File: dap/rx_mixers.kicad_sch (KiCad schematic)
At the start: 2 parts, among them U7 SN74CBT3253, U8 SN74CBT3253

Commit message: general setup
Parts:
- removed U7, U8: SN74CBT3253, symbol Analog_Switch:SN74CBT3253
- added C1, C2: 47u, Capacitor_SMD:C_0805_2012Metric_Pad1.18x1.45mm_HandSolder, symbol Device:C_Polarized_Small_US
- added C10, C11, C16, C3, C4, C5, C6, C7, C8, C9: 0.1u, Capacitor_SMD:C_0805_2012Metric_Pad1.18x1.45mm_HandSolder, symbol Device:C_Small
- added C12, C13, C14, C15, C17, C18, C19, C20: 0.068u, Capacitor_SMD:C_0805_2012Metric_Pad1.18x1.45mm_HandSolder, symbol Device:C_Small
- added H1, H2, H3, H4: MountingHole, MountingHole:MountingHole_3.2mm_M3, symbol Mechanical:MountingHole
- added J12: Conn_01x05_Pin, Connector_PinHeader_2.54mm:PinHeader_1x05_P2.54mm_Vertical, symbol Connector:Conn_01x05_Pin
- added J13: I Channel SMA, Connector_Coaxial:SMA_Amphenol_132289_EdgeMount, symbol Connector:Conn_Coaxial
- added J14: Q Channel SMA, Connector_Coaxial:SMA_Amphenol_132289_EdgeMount, symbol Connector:Conn_Coaxial
- added J15: IF_input, Connector_Coaxial:SMA_Amphenol_132289_EdgeMount, symbol Connector:Conn_Coaxial
- added J16: rf_test, Connector_PinHeader_2.54mm:PinHeader_1x02_P2.54mm_Vertical, symbol Connector:Conn_01x02_Pin
- added J17: I_clk_test, Connector_PinHeader_2.54mm:PinHeader_1x02_P2.54mm_Vertical, symbol Connector:Conn_01x02_Pin
- added J18: Q_clk_test, Connector_PinHeader_2.54mm:PinHeader_1x02_P2.54mm_Vertical, symbol Connector:Conn_01x02_Pin
- added J19: Rx_Q_channel, Connector_Audio:Jack_3.5mm_CUI_SJ-3523-SMT_Horizontal, symbol audiojack3:AudioJack3
- added J20: Rx_I_channel, Connector_Audio:Jack_3.5mm_CUI_SJ-3523-SMT_Horizontal, symbol audiojack3:AudioJack3
- added J21: Tx_Q_channel, Connector_Audio:Jack_3.5mm_CUI_SJ-3523-SMT_Horizontal, symbol audiojack3:AudioJack3
- added J22: Tx_I_channel, Connector_Audio:Jack_3.5mm_CUI_SJ-3523-SMT_Horizontal, symbol audiojack3:AudioJack3
- added R1, R2: 2.2k, Resistor_SMD:R_0805_2012Metric_Pad1.20x1.40mm_HandSolder, symbol Device:R_Small_US
- added R3, R5, R6, R7: 1M, Resistor_SMD:R_0805_2012Metric_Pad1.20x1.40mm_HandSolder, symbol Device:R_Small_US
- added R4: 100, Resistor_SMD:R_0805_2012Metric_Pad1.20x1.40mm_HandSolder, symbol Device:R_Small_US
- added TR1: ADT4-6T, RF_Mini-Circuits:Mini-Circuits_CD637_H5.23mm, symbol Transformer:ADT4-6T
- added U11, U12, U13, U14: NC7SVU04P5X, Package_TO_SOT_SMD:SOT-353_SC-70-5, symbol 74xGxx:NC7SVU04P5X
- added U15, U16: SN74CBT3253, Package_SO:SOIC-16_3.9x9.9mm_P1.27mm, symbol Analog_Switch:SN74CBT3253
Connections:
- new net: C20.2, J22.T, U16.13 (2B4), U16.6 (1B1)
- new net: C12.2, J20.R, U15.10 (2B1), U15.3 (1B4)
- new net: C11.1, J15.1 (In), J16.1 (Pin_1)
- new net: C17.2, J22.R, U16.10 (2B1), U16.3 (1B4)
- new net: C13.2, J19.R, U15.11 (2B2), U15.4 (1B3)
- new net: C14.2, J19.T, U15.12 (2B3), U15.5 (1B2)
- new net: C15.2, J20.T, U15.13 (2B4), U15.6 (1B1)
- new net: TR1.4, U15.7 (1A), U16.7 (1A)
- new net: TR1.6, U15.9 (2A), U16.9 (2A)
- new net: C8.1, R6.1, U12.4
- new net: C6.2, R6.2, U12.2
- new net: C8.2, R7.2, U14.2
- new net: C19.2, J21.T, U16.12 (2B3), U16.5 (1B2)
- new net: C7.1, R3.1, U11.4
- new net: C7.2, R5.2, U13.2
- new net: C5.2, R3.2, U11.2
- new net: C5.1, J13.1 (In)
- new net: C18.2, J21.R, U16.11 (2B2), U16.4 (1B3)
- new net: C11.2, TR1.3
- new net: C6.1, J14.1 (In)
- new net +3.3V: C1.1, J12.2 (Pin_2), R1.1, R4.2
- new net +5V: C16.1, C9.1, J12.1 (Pin_1), U15.16 (VCC), U16.16 (VCC)
- new net GND: C1.2, C10.2, C12.1, C13.1, C14.1, C15.1, C16.2, C17.1, C18.1, C19.1, C2.2, C20.1, C3.2, C4.2, C9.2, J12.5 (Pin_5), J13.2 (Ext), J14.2 (Ext), J15.2 (Ext), J16.2 (Pin_2), J17.2 (Pin_2), J18.2 (Pin_2), J19.S, J20.S, J21.S, J22.S, R2.1, TR1.1, U11.3 (GND), U12.3 (GND), U13.3 (GND), U14.3 (GND), U15.8 (GND), U16.8 (GND)
- new net I_square: J17.1 (Pin_1), R5.1, U13.4, U15.14 (S0), U16.14 (S0)
- new net Q_square: J18.1 (Pin_1), R7.1, U14.4, U15.2 (S1), U16.2 (S1)
- new net Rx_control: J12.4 (Pin_4), U15.1 (1~{OE}), U15.15 (2~{OE})
- new net Tx_control: J12.3 (Pin_3), U16.1 (1~{OE}), U16.15 (2~{OE})
- new net V_inverter: C2.1, C3.1, C4.1, R4.1, U11.5 (VCC), U12.5 (VCC), U13.5 (VCC), U14.5 (VCC)
- new net bias: C10.1, R1.2, R2.2, TR1.5
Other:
- note added: "Detector Bias Circuit"
- note added: "Inverter Power"
- note added: "Power Flags"
- note added: "Power and Control"
- note added: "Quadrature Clocks"
- note added: "Receive Mixer"
- note added: "Transmit Mixer"

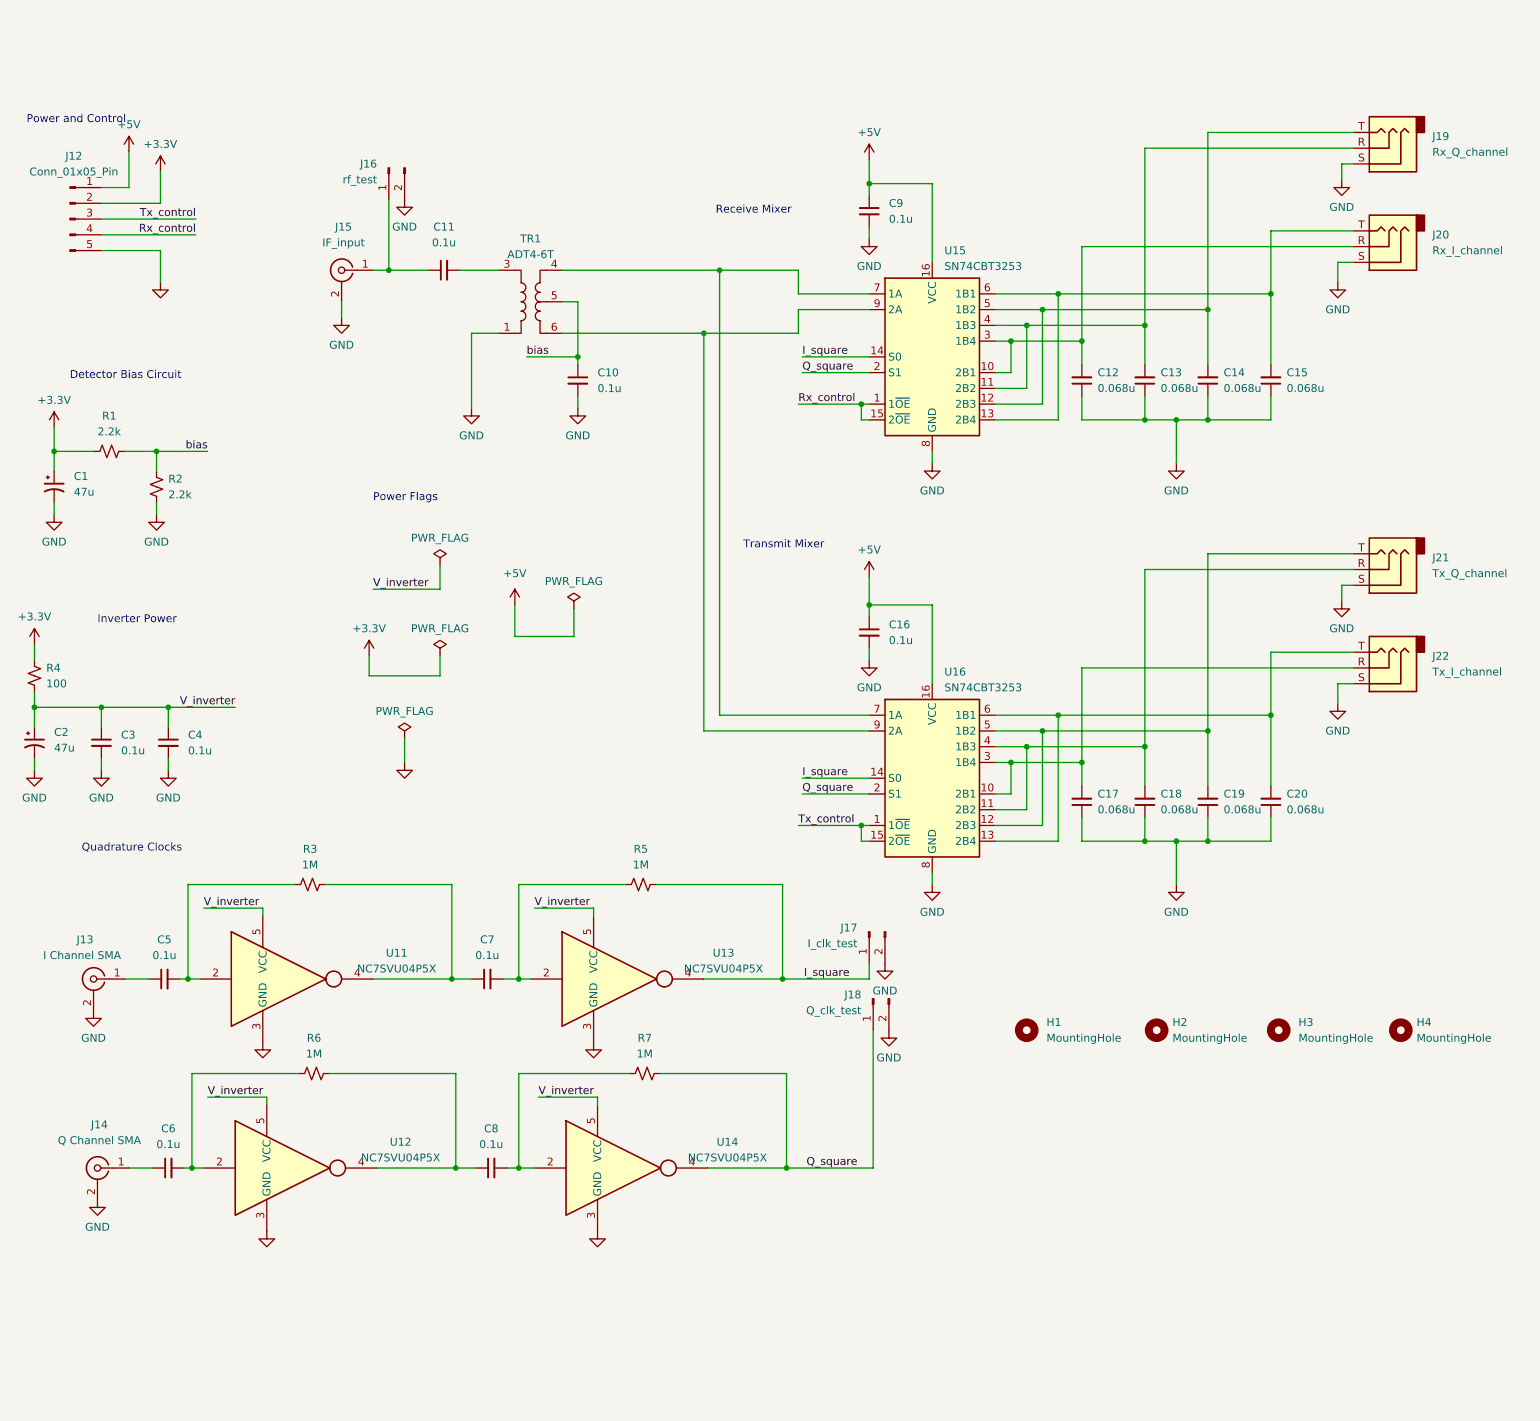
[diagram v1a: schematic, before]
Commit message: selected clocking scheme
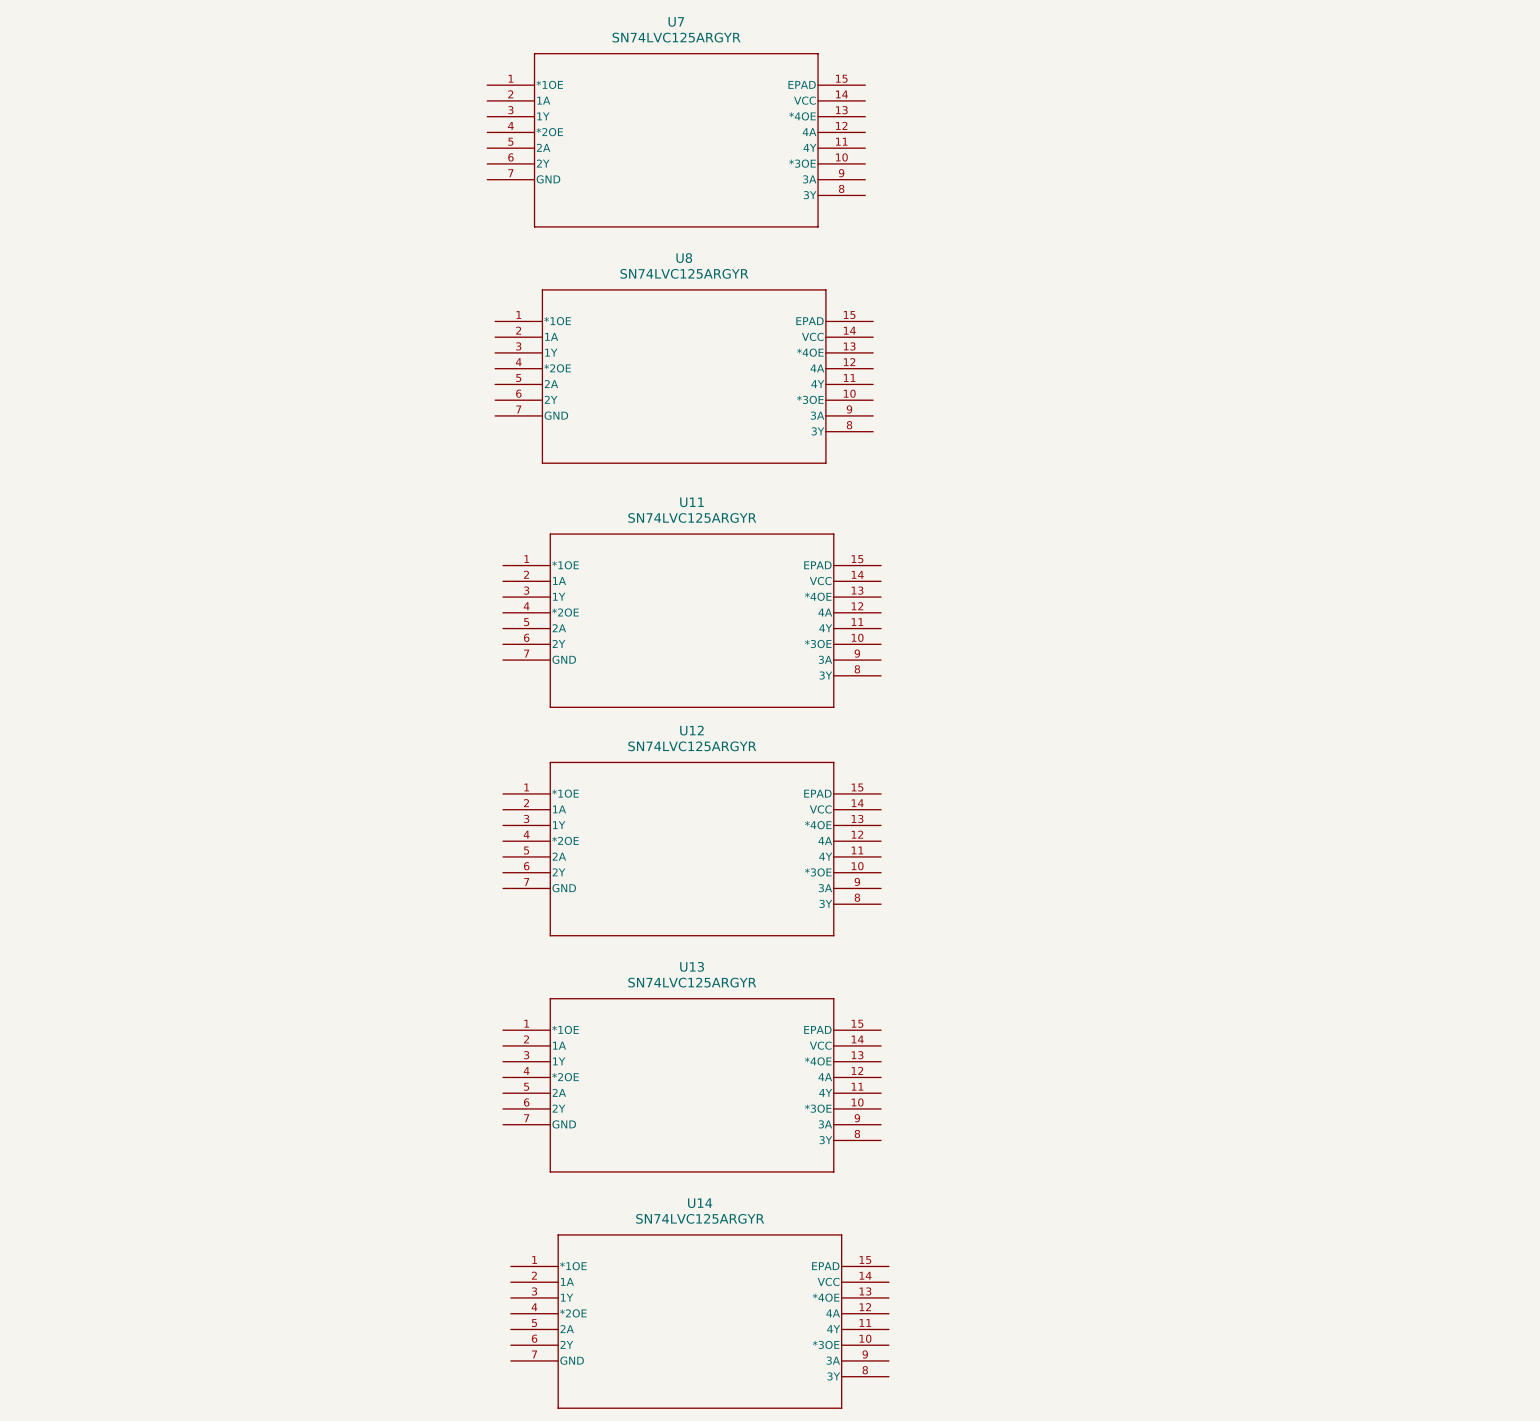
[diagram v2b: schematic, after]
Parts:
- removed C1, C2: 47u, Capacitor_SMD:C_0805_2012Metric_Pad1.18x1.45mm_HandSolder, symbol Device:C_Polarized_Small_US
- removed C10, C11, C16, C3, C4, C5, C6, C7, C8, C9: 0.1u, Capacitor_SMD:C_0805_2012Metric_Pad1.18x1.45mm_HandSolder, symbol Device:C_Small
- removed C12, C13, C14, C15, C17, C18, C19, C20: 0.068u, Capacitor_SMD:C_0805_2012Metric_Pad1.18x1.45mm_HandSolder, symbol Device:C_Small
- removed H1, H2, H3, H4: MountingHole, MountingHole:MountingHole_3.2mm_M3, symbol Mechanical:MountingHole
- removed J12: Conn_01x05_Pin, Connector_PinHeader_2.54mm:PinHeader_1x05_P2.54mm_Vertical, symbol Connector:Conn_01x05_Pin
- removed J13: I Channel SMA, Connector_Coaxial:SMA_Amphenol_132289_EdgeMount, symbol Connector:Conn_Coaxial
- removed J14: Q Channel SMA, Connector_Coaxial:SMA_Amphenol_132289_EdgeMount, symbol Connector:Conn_Coaxial
- removed J15: IF_input, Connector_Coaxial:SMA_Amphenol_132289_EdgeMount, symbol Connector:Conn_Coaxial
- removed J16: rf_test, Connector_PinHeader_2.54mm:PinHeader_1x02_P2.54mm_Vertical, symbol Connector:Conn_01x02_Pin
- removed J17: I_clk_test, Connector_PinHeader_2.54mm:PinHeader_1x02_P2.54mm_Vertical, symbol Connector:Conn_01x02_Pin
- removed J18: Q_clk_test, Connector_PinHeader_2.54mm:PinHeader_1x02_P2.54mm_Vertical, symbol Connector:Conn_01x02_Pin
- removed J19: Rx_Q_channel, Connector_Audio:Jack_3.5mm_CUI_SJ-3523-SMT_Horizontal, symbol audiojack3:AudioJack3
- removed J20: Rx_I_channel, Connector_Audio:Jack_3.5mm_CUI_SJ-3523-SMT_Horizontal, symbol audiojack3:AudioJack3
- removed J21: Tx_Q_channel, Connector_Audio:Jack_3.5mm_CUI_SJ-3523-SMT_Horizontal, symbol audiojack3:AudioJack3
- removed J22: Tx_I_channel, Connector_Audio:Jack_3.5mm_CUI_SJ-3523-SMT_Horizontal, symbol audiojack3:AudioJack3
- removed R1, R2: 2.2k, Resistor_SMD:R_0805_2012Metric_Pad1.20x1.40mm_HandSolder, symbol Device:R_Small_US
- removed R3, R5, R6, R7: 1M, Resistor_SMD:R_0805_2012Metric_Pad1.20x1.40mm_HandSolder, symbol Device:R_Small_US
- removed R4: 100, Resistor_SMD:R_0805_2012Metric_Pad1.20x1.40mm_HandSolder, symbol Device:R_Small_US
- removed TR1: ADT4-6T, RF_Mini-Circuits:Mini-Circuits_CD637_H5.23mm, symbol Transformer:ADT4-6T
- removed U11, U12, U13, U14: NC7SVU04P5X, Package_TO_SOT_SMD:SOT-353_SC-70-5, symbol 74xGxx:NC7SVU04P5X
- removed U15, U16: SN74CBT3253, Package_SO:SOIC-16_3.9x9.9mm_P1.27mm, symbol Analog_Switch:SN74CBT3253
- added U11, U12, U13, U14, U7, U8: SN74LVC125ARGYR, RGY14_2P05X2P05, symbol SN74LVC125A:SN74LVC125ARGYR
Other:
- note removed: "Detector Bias Circuit"
- note removed: "Inverter Power"
- note removed: "Power Flags"
- note removed: "Power and Control"
- note removed: "Quadrature Clocks"
- note removed: "Receive Mixer"
- note removed: "Transmit Mixer"
